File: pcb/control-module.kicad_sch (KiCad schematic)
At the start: 27 parts, among them J1 Screw_Terminal_01x06, J2 Conn_01x07_Pin, SW1 SW_DIP_x04, U1 TPS2116DRL

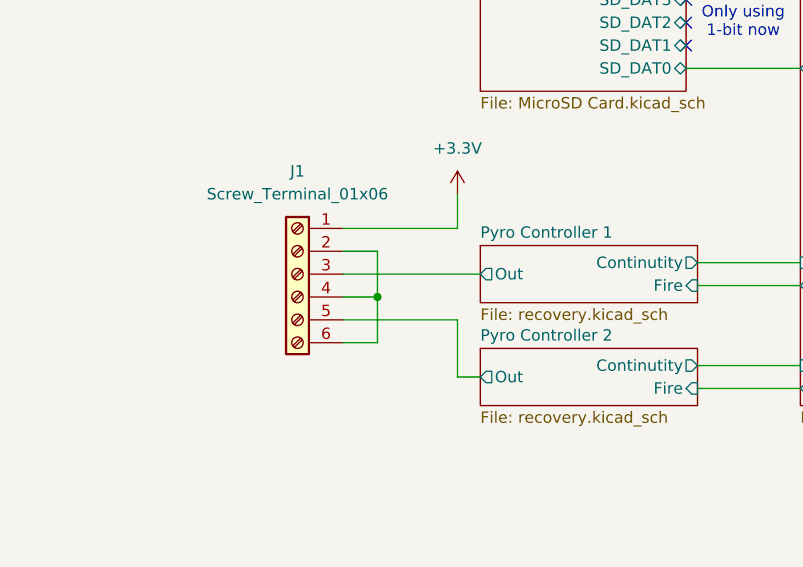
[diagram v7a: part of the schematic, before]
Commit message: Updated PCB Layout, changed to 4 layer board
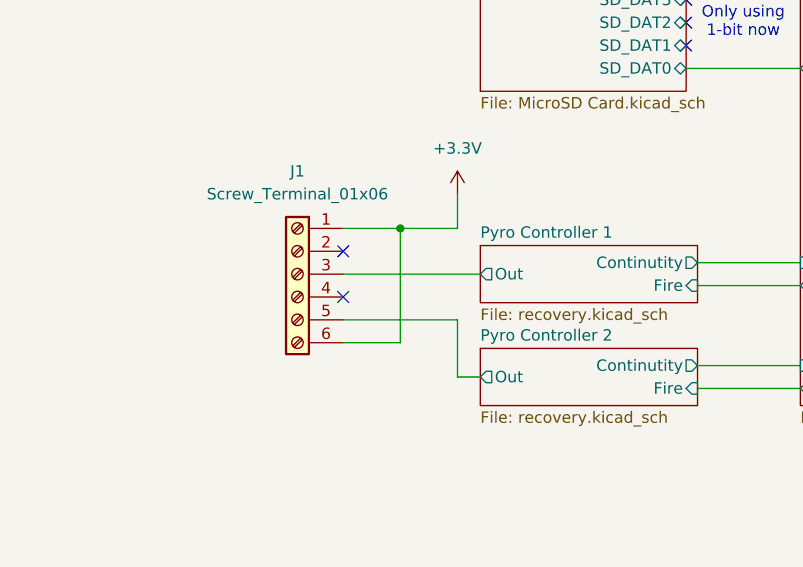
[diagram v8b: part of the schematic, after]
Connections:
- net +3.3V: now also J1.6 (Pin_6)
- now unconnected: J1.2 (Pin_2), J1.4 (Pin_4)
- no-connect marks 4 -> 6
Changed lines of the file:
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@@
 	)
 	(junction
-		(at 58.42 113.03)
+		(at 60.96 105.41)
 		(diameter 0)
 		(color 0 0 0 0)
@@
 	)
 	(no_connect
+		(at 54.61 107.95)
+	)
+	(no_connect
 		(at 92.71 85.09)
 	)
@@
 		(at 217.17 78.74)
 	)
+	(no_connect
+		(at 54.61 113.03)
+	)
 	(wire
 		(pts
@@
 	(wire
 		(pts
+			(xy 60.96 105.41) (xy 67.31 105.41)
+		)
+		(stroke
+			(width 0)
+			(type default)
+		)
+	)
+	(wire
+		(pts
 			(xy 67.31 121.92) (xy 67.31 115.57)
 		)
@@
 	(wire
 		(pts
-			(xy 58.42 118.11) (xy 58.42 113.03)
-		)
-		(stroke
-			(width 0)
-			(type default)
-		)
-	)
-	(wire
-		(pts
 			(xy 149.86 21.59) (xy 149.86 26.67)
 		)
@@
 	(wire
 		(pts
+			(xy 54.61 118.11) (xy 60.96 118.11)
+		)
+		(stroke
+			(width 0)
+			(type default)
+		)
+	)
+	(wire
+		(pts
 			(xy 177.8 158.75) (xy 194.31 158.75)
 		)
@@
 	(wire
 		(pts
-			(xy 54.61 113.03) (xy 58.42 113.03)
-		)
-		(stroke
-			(width 0)
-			(type default)
-		)
-	)
-	(wire
-		(pts
 			(xy 142.24 116.84) (xy 158.75 116.84)
 		)
@@
 	(wire
 		(pts
-			(xy 54.61 118.11) (xy 58.42 118.11)
-		)
-		(stroke
-			(width 0)
-			(type default)
-		)
-	)
-	(wire
-		(pts
 			(xy 74.93 22.86) (xy 74.93 26.67)
 		)
@@
 	(wire
 		(pts
-			(xy 54.61 107.95) (xy 58.42 107.95)
-		)
-		(stroke
-			(width 0)
-			(type default)
-		)
-	)
-	(wire
-		(pts
 			(xy 232.41 73.66) (xy 241.3 73.66)
 		)
@@
 	(wire
 		(pts
-			(xy 54.61 105.41) (xy 67.31 105.41)
+			(xy 54.61 105.41) (xy 60.96 105.41)
 		)
 		(stroke
@@
 	(wire
 		(pts
-			(xy 58.42 113.03) (xy 58.42 107.95)
-		)
-		(stroke
-			(width 0)
-			(type default)
-		)
-	)
-	(wire
-		(pts
 			(xy 185.42 139.7) (xy 185.42 140.97)
 		)
@@
 		)
 		(stroke
+			(width 0)
+			(type default)
+		)
+	)
+	(wire
+		(pts
+			(xy 60.96 118.11) (xy 60.96 105.41)
+		)
+		(stroke
